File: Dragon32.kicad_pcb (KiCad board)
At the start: 2 copper layers, 120.2 x 78.9 mm, 59 parts, among them IC1 74LS273N, IC10 74LS32N, IC11 74LS123N, IC12 LM1889N, IC13 2318, IC15 MC14053, IC2 MC6847, IC3 74LS00N, IC4 74LS20N, IC5 74LS86AN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

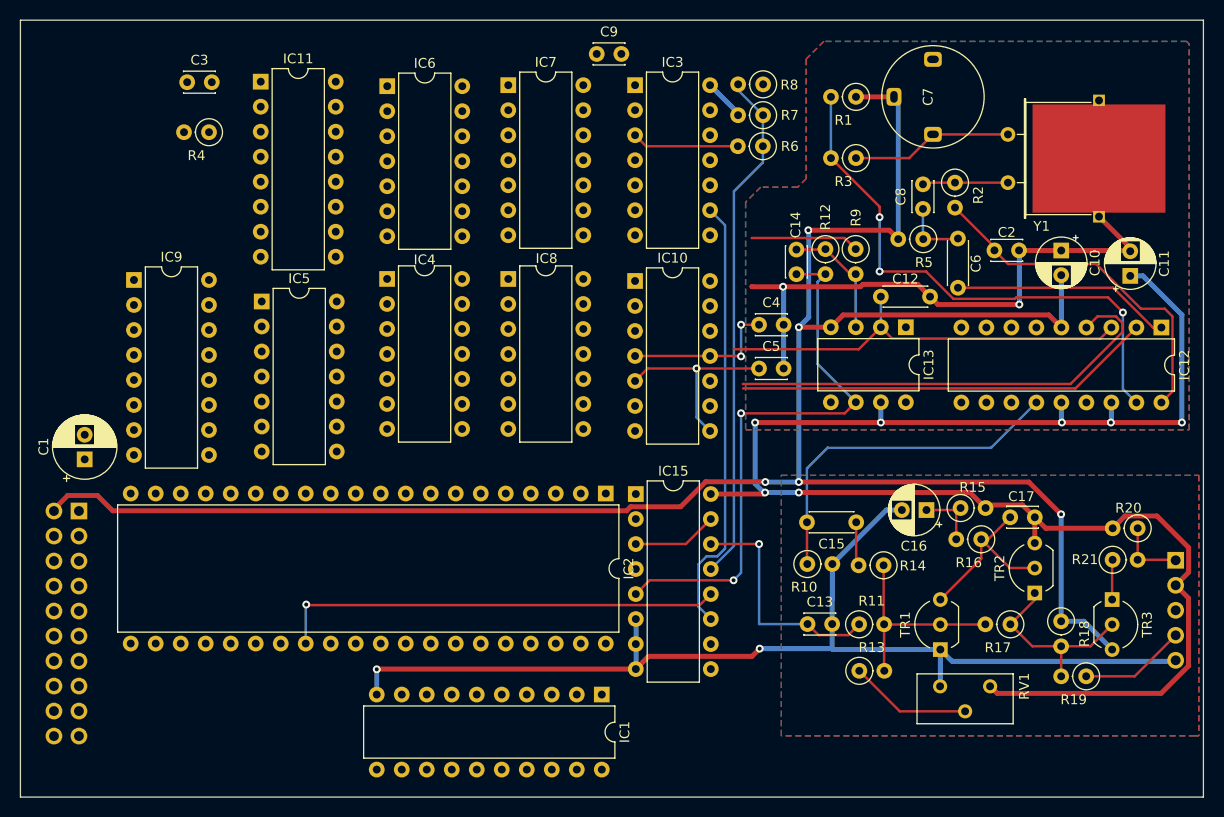
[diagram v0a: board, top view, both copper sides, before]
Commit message: fix missing css and fs signals
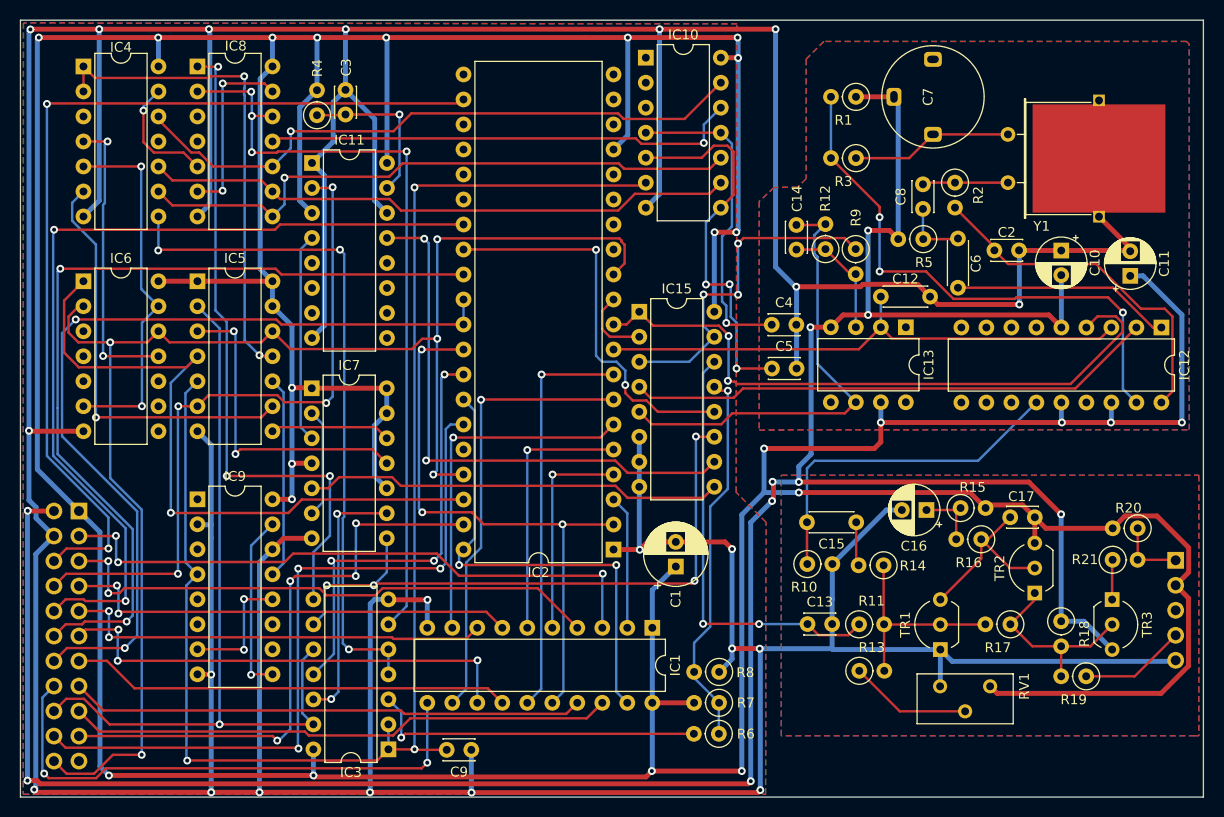
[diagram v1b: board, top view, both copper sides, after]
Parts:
- J1: value Board interconnect -> Board Interconnect Male; footprint Connector_PinHeader_2.54mm:PinHeader_2x10_P2.54mm_Vertical -> Connector_PinHeader_2.54mm:PinHeader_2x11_P2.54mm_Vertical
- moved IC3 72.0 mm to (269.6, 124.4), turned to 180 degrees
- moved C9 71.8 mm to (278.1, 124.4), turned to 180 degrees
- moved C1 61.0 mm to (298.8, 105.8)
- moved R6 59.9 mm to (303.2, 122.8)
- moved R8 59.9 mm to (303.2, 116.5)
- moved R7 59.9 mm to (303.2, 119.6)
- moved IC8 38.2 mm to (250.2, 55.0)
- moved IC4 37.6 mm to (238.7, 55.0)
- moved IC7 36.7 mm to (261.8, 87.7)
- moved IC6 36.7 mm to (238.7, 76.8)
- moved IC9 23.2 mm to (250.2, 99.0)
- moved IC10 22.7 mm to (295.8, 54.1)
- moved IC15 18.5 mm to (295.1, 79.9)
- moved C3 16.4 mm to (265.3, 59.9), turned to 90 degrees
- moved R4 11.1 mm to (262.4, 59.9), turned to 90 degrees
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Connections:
- J1 pad 19: unconnected-(J1-Pin_19-Pad19) -> CSS
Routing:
- net GND: track 170.1 -> 642.3 mm, vias 4 -> 21
- net +5V: track 168.7 -> 592.7 mm, vias 7 -> 23
- net /LINE PULSES: track 0.00 -> 150.2 mm, vias 0 -> 3
- net ~{FS}: track 0.00 -> 147.5 mm, vias 0 -> 5
- net DA0: track 0.00 -> 96.3 mm, vias 0 -> 2
- net GM2: track 0.00 -> 90.5 mm, vias 0 -> 2
- net GM1: track 0.00 -> 88.6 mm, vias 0 -> 2
- net GM0: track 0.00 -> 87.5 mm, vias 0 -> 2
- net VCLK: track 0.00 -> 79.9 mm, vias 0 -> 1
- net Net-(IC8A-MR): track 0.00 -> 78.4 mm, vias 0 -> 4
- net ~{A}/G: track 0.00 -> 74.5 mm, vias 0 -> 3
- net ~{NHS}: track 0.00 -> 70.3 mm, vias 0 -> 4
- net ~{HS}: track 0.00 -> 70.0 mm, vias 0 -> 1
- net Net-(IC3-Pad4): track 0.00 -> 69.6 mm, vias 0 -> 3
- net /~{VCLK}: track 0.00 -> 68.0 mm, vias 0 -> 3
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
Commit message: partial conversion
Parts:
- C1: footprint Capacitor_THT:CP_Radial_D6.3mm_P2.50mm -> Capacitor_SMD:CP_Elec_6.3x5.8
- C10, C11: footprint Capacitor_THT:CP_Radial_D5.0mm_P2.50mm -> Capacitor_SMD:CP_Elec_5x5.8
- C12, C15, C6: footprint Capacitor_THT:C_Disc_D4.3mm_W1.9mm_P5.00mm -> Capacitor_SMD:C_0805_2012Metric_Pad1.18x1.45mm_HandSolder
- C13, C14, C17, C2, C3, C4, C5, C8, C9: footprint Capacitor_THT:C_Disc_D3.0mm_W2.0mm_P2.50mm -> Capacitor_SMD:C_0805_2012Metric_Pad1.18x1.45mm_HandSolder
- C16: footprint Capacitor_THT:CP_Radial_D5.0mm_P2.50mm -> Capacitor_SMD:CP_Elec_4x5.4
- IC1: value 74LS273N -> 74HCT273; footprint Package_DIP:DIP-20_W7.62mm -> Package_SO:TSSOP-20_4.4x6.5mm_P0.65mm
- IC10: value 74LS32N -> 74HCT32; footprint Package_DIP:DIP-14_W7.62mm -> Package_SO:SOIC-16_3.9x9.9mm_P1.27mm
- IC11: footprint Package_DIP:DIP-16_W7.62mm -> Package_SO:SOIC-16_3.9x9.9mm_P1.27mm
- IC15: value MC14053 -> CD4053; footprint Package_DIP:DIP-16_W7.62mm -> Package_SO:SOIC-16_3.9x9.9mm_P1.27mm
- IC3: value 74LS00N -> 74HCT00; footprint Package_DIP:DIP-14_W7.62mm -> Package_SO:SOIC-14_3.9x8.7mm_P1.27mm
- IC4: value 74LS20N -> 74HCT20; footprint Package_DIP:DIP-14_W7.62mm -> Package_SO:SOIC-14_3.9x8.7mm_P1.27mm
- IC5: value 74LS86AN -> 74HCT86; footprint Package_DIP:DIP-14_W7.62mm -> Package_SO:SOIC-14_3.9x8.7mm_P1.27mm
- IC6, IC8: value 74LS393N -> 74HCT393; footprint Package_DIP:DIP-14_W7.62mm -> Package_SO:SOIC-14_3.9x8.7mm_P1.27mm
- IC7: footprint Package_DIP:DIP-14_W7.62mm -> Package_SO:SOIC-14_3.9x8.7mm_P1.27mm
- IC9: value 74LS390 -> 74HCT390; footprint Package_DIP:DIP-16_W7.62mm -> Package_SO:SOIC-16_3.9x9.9mm_P1.27mm
- R1, R10, R11, R12, R13, R14, R15, R16, R17, R18, R19, R2, R20, R21, R3, R4, R5, R6, R7, R8, R9: footprint Resistor_THT:R_Axial_DIN0207_L6.3mm_D2.5mm_P2.54mm_Vertical -> Resistor_SMD:R_0805_2012Metric_Pad1.20x1.40mm_HandSolder
- moved IC1 46.6 mm to (251.0, 122.2), turned to 0 degrees
- moved IC3 19.2 mm to (288.8, 123.6), turned to -90 degrees
- moved IC10 17.8 mm to (297.9, 71.8)
- moved IC8 17.0 mm to (250.3, 72.0)
- moved IC4 16.5 mm to (239.2, 71.5)
- moved C9 16.0 mm to (292.4, 117.3)
- moved IC7 14.3 mm to (262.4, 102.0)
- moved IC11 14.2 mm to (261.6, 79.0)
- moved IC2 13.1 mm to (287.0, 116.0)
- moved IC9 10.8 mm to (251.0, 109.7)
- moved IC6 10.6 mm to (239.5, 87.4)
- moved IC5 10.6 mm to (250.3, 87.4)
- moved IC15 8.70 mm to (297.9, 88.1)
- moved C5 8.59 mm to (313.3, 78.5)
- moved C3 8.19 mm to (261.2, 67.0)
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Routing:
- net GND: track 642.3 -> 226.1 mm, vias 21 -> 15
- net +5V: track 592.7 -> 239.4 mm, vias 23 -> 3
- net ~{FS}: track 147.5 -> 0.00 mm, vias 5 -> 0
- net /LINE PULSES: track 150.2 -> 7.69 mm, vias 3 -> 0
- net -5V: track 261.8 -> 138.0 mm, vias 10 -> 5
- net DA0: track 96.3 -> 0.00 mm, vias 2 -> 0
- net GM2: track 90.5 -> 0.00 mm, vias 2 -> 0
- net GM1: track 88.6 -> 0.00 mm, vias 2 -> 0
- net GM0: track 87.5 -> 0.00 mm, vias 2 -> 0
- net VCLK: track 79.9 -> 0.00 mm, vias 1 -> 0
- net Net-(IC8A-MR): track 78.4 -> 0.00 mm, vias 4 -> 0
- net ~{A}/G: track 74.5 -> 0.00 mm, vias 3 -> 0
- net ~{NHS}: track 70.3 -> 0.00 mm, vias 4 -> 0
- net ~{HS}: track 70.0 -> 0.00 mm, vias 1 -> 0
- net Net-(IC3-Pad4): track 69.6 -> 0.00 mm, vias 3 -> 0
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
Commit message: complete traces
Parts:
- moved C1 39.6 mm to (293.3, 67.7), turned to 0 degrees
- moved IC1 13.1 mm to (248.8, 109.2)
- moved IC9 11.0 mm to (248.7, 99.0)
- moved R9 9.20 mm to (314.5, 79.1)
- moved IC10 7.85 mm to (297.9, 79.6)
- moved C12 7.21 mm to (319.5, 84.5)
- moved R12 7.21 mm to (318.9, 79.1)
- moved R2 7.21 mm to (328.0, 74.0)
- moved R5 7.21 mm to (324.1, 79.7)
- moved C4 7.21 mm to (314.1, 83.5)
- moved C6 7.21 mm to (328.3, 80.7)
- moved C8 7.21 mm to (324.7, 74.1)
- moved IC12 7.21 mm to (349.0, 88.7)
- moved IC13 7.21 mm to (323.0, 88.6)
- moved R1 7.21 mm to (317.9, 66.1)
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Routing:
- net GND: track 226.1 -> 584.7 mm, vias 15 -> 27
- net +5V: track 239.4 -> 510.9 mm, vias 3 -> 23
- net -5V: track 138.0 -> 277.6 mm, vias 5 -> 6
- net ~{FS}: track 0.00 -> 136.8 mm, vias 0 -> 8
- net VCLK: track 0.00 -> 119.7 mm, vias 0 -> 10
- net /LINE PULSES: track 7.69 -> 114.7 mm, vias 0 -> 7
- net Net-(IC3-Pad4): track 0.00 -> 92.7 mm, vias 0 -> 4
- net /~{VCLK}: track 0.00 -> 91.5 mm, vias 0 -> 4
- net LUM CONTROL: track 0.00 -> 88.7 mm, vias 0 -> 4
- net Net-(IC8A-MR): track 0.00 -> 88.1 mm, vias 0 -> 4
- net DA0: track 0.00 -> 77.4 mm, vias 0 -> 2
- net ~{HS}: track 0.00 -> 75.0 mm, vias 0 -> 6
- net Net-(IC1-Q0): track 0.00 -> 73.0 mm, vias 0 -> 4
- net Net-(IC4-Pad1): track 0.00 -> 68.0 mm, vias 0 -> 4
- net Net-(IC1-Q2): track 0.00 -> 66.7 mm, vias 0 -> 4
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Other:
- board size 120.2 x 78.9 mm -> 120.2 x 69.7 mm

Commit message: fix diff amp wiring
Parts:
- turned C12 to 0 degrees
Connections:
- C14 pad 1: Net-(IC13-+) -> Net-(IC13--)
- IC13 pad 2: CHB -> Net-(IC13--)
- IC13 pad 3: Net-(IC13-+) -> CHB
- R12 pad 1: Net-(IC13-+) -> Net-(IC13--)
- R9 pad 2: Net-(IC13-+) -> Net-(IC13--)
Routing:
- net Net-(IC13-+): track 13.9 -> 0.00 mm
- net Net-(IC13--): track 0.00 -> 13.6 mm
- net CHB: track 70.2 -> 71.6 mm
- net MUX Y: track 37.3 -> 37.9 mm
- net GND: vias 27 -> 26
